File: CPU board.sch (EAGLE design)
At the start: 59 parts, among them U1 74HC245, U10 74HC08, U11 74HC32, U12 SST39SF010, U13 AS6C62256, U14 SST39SF010, U15 SST39SF010, U2 74HC245, U3 74HC245, U4 TL7705, U5 Z80, U6 74HC138, U7 74HC74, U8 74HC11, U9 74HC02

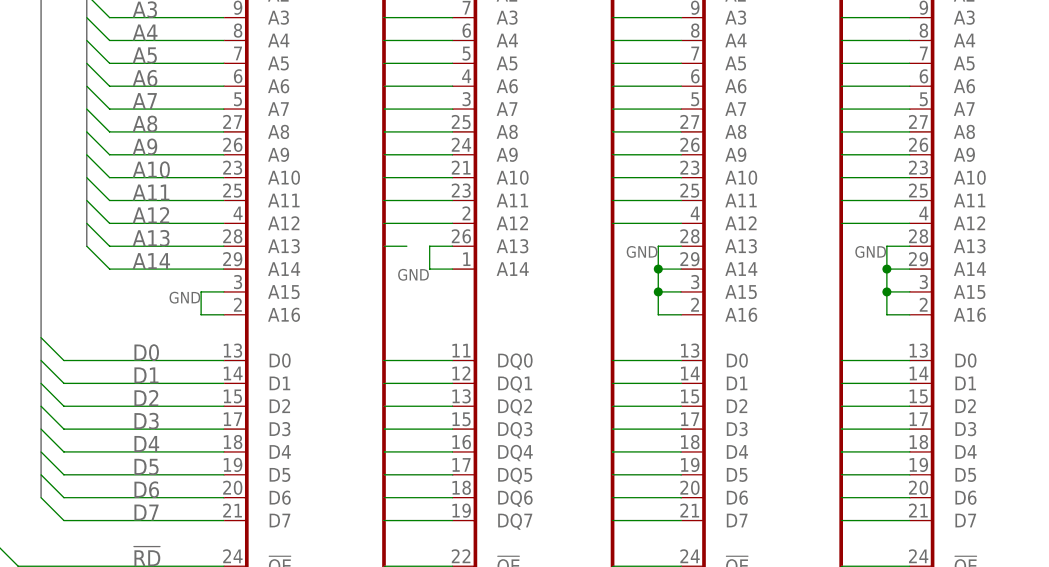
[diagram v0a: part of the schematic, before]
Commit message: Extend A13 to U13
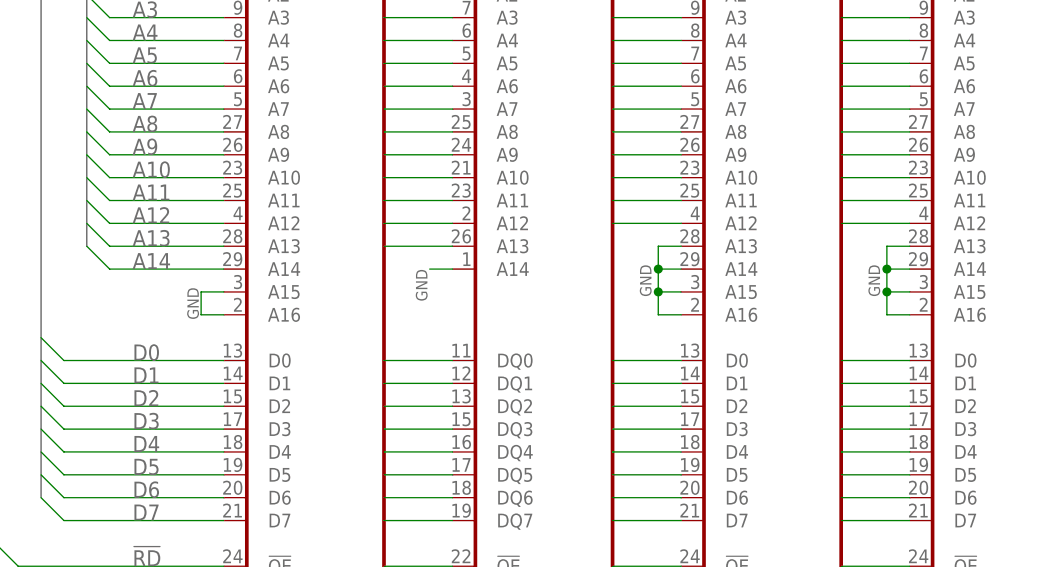
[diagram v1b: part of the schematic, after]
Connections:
- net A13: now also U13G$1.A13
- net GND: no longer U13G$1.A13
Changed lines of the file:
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@@
 <?xml version="1.0" encoding="utf-8"?>
 <!DOCTYPE eagle SYSTEM "eagle.dtd">
-<eagle version="9.5.2">
+<eagle version="9.6.1">
 <drawing>
 <settings>
@@
 GREEN  CPU RUNNING
 RED    CPU HALTED</text>
-<wire x1="317.5" y1="142.24" x2="347.98" y2="142.24" width="0.254" layer="90"/>
-<wire x1="347.98" y1="142.24" x2="347.98" y2="129.54" width="0.254" layer="90"/>
-<wire x1="347.98" y1="129.54" x2="317.5" y2="129.54" width="0.254" layer="90"/>
-<wire x1="317.5" y1="129.54" x2="317.5" y2="142.24" width="0.254" layer="90"/>
 </plain>
 <instances>
@@
 <wire x1="307.34" y1="132.08" x2="304.8" y2="132.08" width="0.1524" layer="91"/>
 <wire x1="304.8" y1="132.08" x2="304.8" y2="129.54" width="0.1524" layer="91"/>
-<label x="304.8" y="132.08" size="1.27" layer="95" rot="R180"/>
-</segment>
-<segment>
-<pinref part="U13" gate="G$1" pin="A14"/>
-<wire x1="332.74" y1="134.62" x2="330.2" y2="134.62" width="0.1524" layer="91"/>
-<label x="330.2" y="134.62" size="1.27" layer="95" rot="R180"/>
-<pinref part="U13" gate="G$1" pin="A13"/>
-<wire x1="332.74" y1="137.16" x2="330.2" y2="137.16" width="0.1524" layer="91"/>
-<wire x1="330.2" y1="137.16" x2="330.2" y2="134.62" width="0.1524" layer="91"/>
+<label x="304.546" y="132.588" size="1.27" layer="95" rot="MR270"/>
 </segment>
 <segment>
@@
 <wire x1="355.6" y1="137.16" x2="355.6" y2="134.62" width="0.1524" layer="91"/>
 <junction x="355.6" y="134.62"/>
-<label x="355.6" y="137.16" size="1.27" layer="95" rot="R180"/>
+<label x="354.838" y="135.128" size="1.27" layer="95" rot="MR270"/>
 </segment>
 <segment>
@@
 <wire x1="381" y1="137.16" x2="381" y2="134.62" width="0.1524" layer="91"/>
 <junction x="381" y="134.62"/>
-<label x="381" y="137.16" size="1.27" layer="95" rot="R180"/>
+<label x="380.238" y="135.128" size="1.27" layer="95" rot="MR270"/>
 </segment>
 <segment>
@@
 <wire x1="-5.08" y1="195.58" x2="-5.08" y2="190.5" width="0.1524" layer="91"/>
 </segment>
+<segment>
+<pinref part="U13" gate="G$1" pin="A14"/>
+<wire x1="332.74" y1="134.62" x2="330.2" y2="134.62" width="0.1524" layer="91"/>
+<label x="329.946" y="134.62" size="1.27" layer="95" rot="MR270"/>
+</segment>
 </net>
 <net name="D0" class="0">
@@
 </segment>
 <segment>
-<wire x1="325.12" y1="137.16" x2="327.66" y2="137.16" width="0.1524" layer="91"/>
-</segment>
-</net>
+<wire x1="325.12" y1="137.16" x2="332.74" y2="137.16" width="0.1524" layer="91"/>
+<pinref part="U13" gate="G$1" pin="A13"/>
+</segment>
+</net>
